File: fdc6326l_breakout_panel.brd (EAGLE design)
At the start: 41.1 x 42.7 mm, 105 parts, among them U1 FDC6326L, U10 FDC6326L, U11 FDC6326L, U12 FDC6326L, U13 FDC6326L, U14 FDC6326L, U15 FDC6326L, U2 FDC6326L, U3 FDC6326L, U4 FDC6326L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

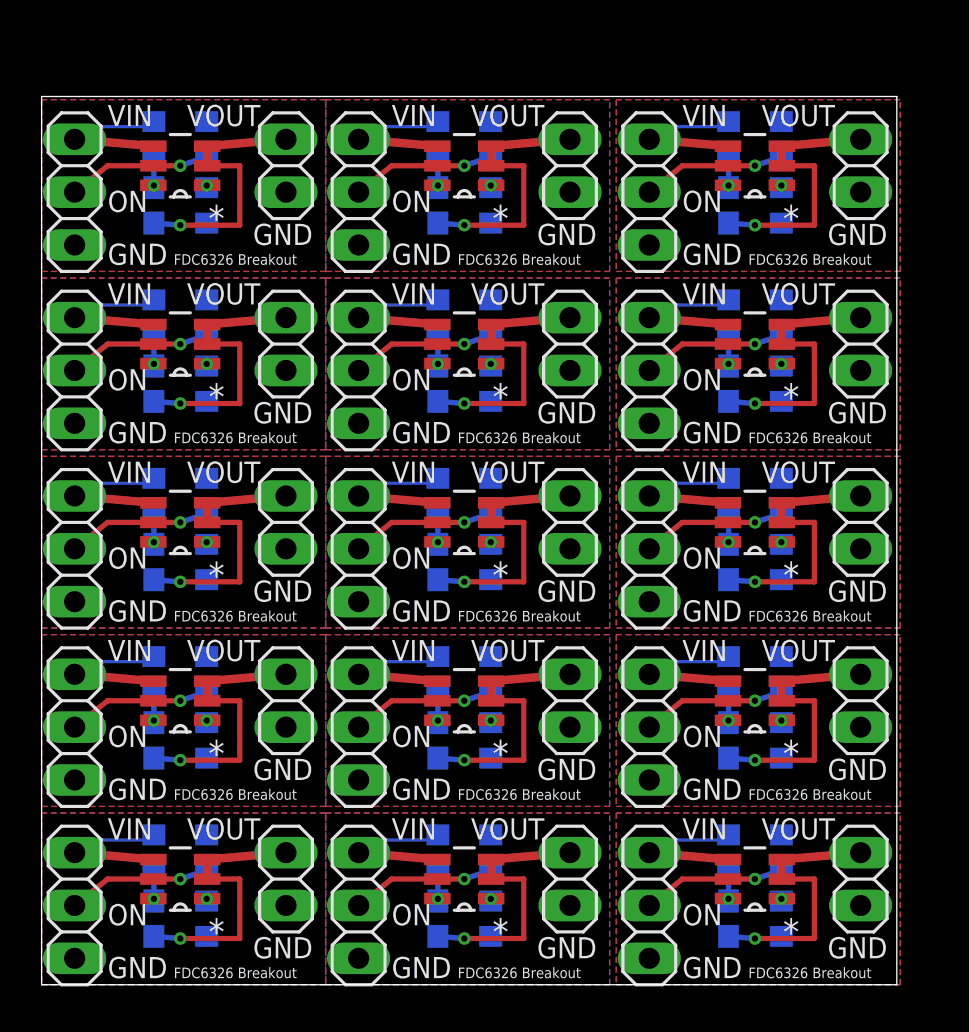
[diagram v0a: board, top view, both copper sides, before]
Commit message: less tigh spacing
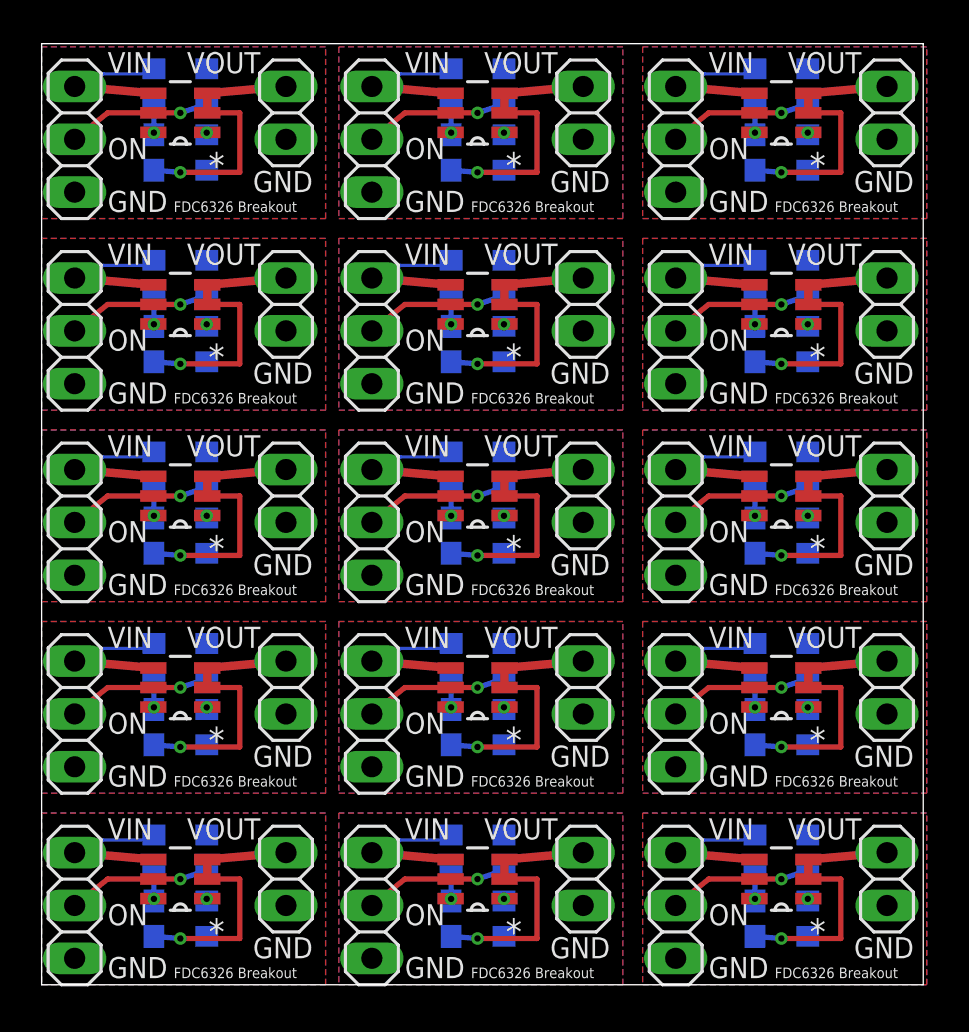
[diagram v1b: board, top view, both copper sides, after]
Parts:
- moved JP30 2.84 mm to (40.6, 41.9)
- moved U15 2.84 mm to (35.6, 41.9)
- moved JP29 2.84 mm to (30.5, 40.6)
- moved C15 2.84 mm to (34.3, 40.0)
- moved PD14 2.84 mm to (36.8, 43.2)
- moved R29 2.84 mm to (34.3, 43.2)
- moved R30 2.84 mm to (36.8, 40.0)
- moved JP28 2.62 mm to (26.0, 41.9)
- moved PD13 2.62 mm to (22.2, 43.2)
- moved R28 2.62 mm to (22.2, 40.0)
- moved JP27 2.62 mm to (15.9, 40.6)
- moved C14 2.62 mm to (19.7, 40.0)
- moved R27 2.62 mm to (19.7, 43.2)
- moved U14 2.62 mm to (21.0, 41.9)
- moved C13 2.54 mm to (5.40, 40.0)
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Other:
- board size 41.1 x 42.7 mm -> 42.4 x 45.2 mm
